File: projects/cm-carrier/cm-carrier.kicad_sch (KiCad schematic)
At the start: 0 parts

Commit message: cm-carrier: power sheet (XA 5V input, TPS62132 3.3V/3A for LTE)
Co-Authored-By: Claude Opus 5.5 <noreply@anthropic.com>
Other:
- added sheet Power (power.kicad_sch)
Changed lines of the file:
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@@
 	(generator_version "10.0")
 	(paper "A4")
+  (sheet
+    (at 30 30)
+    (size 40 25)
+    (exclude_from_sim no)
+    (in_bom yes)
+    (on_board yes)
+    (dnp no)
+    (fields_autoplaced yes)
+    (stroke (width 0.1524) (type solid))
+    (fill (color 0 0 0 0.0))
+    (property "Sheetname" "Power"
+      (at 30 29.365 0)
+      (show_name no)
+      (do_not_autoplace no)
+      (effects (font (size 1.27 1.27)) (justify left bottom))
+    )
+    (property "Sheetfile" "power.kicad_sch"
+      (at 30 55.635 0)
+      (show_name no)
+      (do_not_autoplace no)
+      (effects (font (size 1.27 1.27)) (justify left top))
+    )
+    (instances
+      (project "cm-carrier"
+        (path "/a976657b-65a0-4cc4-bafb-6280c56b6145" (page "2"))
+      )
+    )
+  )
+  (sheet_instances
+    (path "/"
+      (page "1")
+    )
+  )
+  (embedded_fonts no)
 )

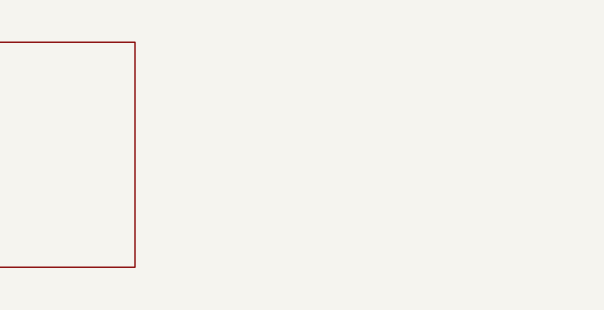
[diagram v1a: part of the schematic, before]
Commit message: cm-carrier: CM sheet (CM4/CM5 module, debug UART, ACT LED, power button)
Co-Authored-By: Claude Opus 5.5 <noreply@anthropic.com>
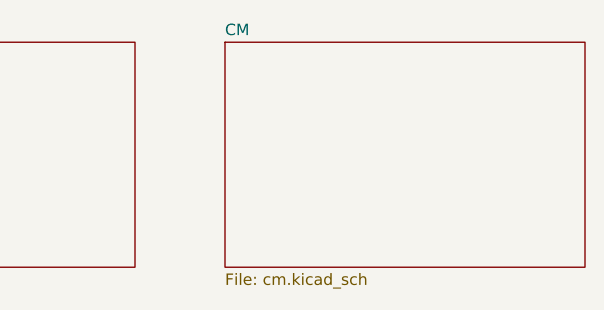
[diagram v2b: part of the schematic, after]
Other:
- added sheet CM (cm.kicad_sch)
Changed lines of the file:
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@@
+    )
+  )
+  (sheet
+    (at 80 30)
+    (size 40 25)
+    (exclude_from_sim no)
+    (in_bom yes)
+    (on_board yes)
+    (dnp no)
+    (fields_autoplaced yes)
+    (stroke (width 0.1524) (type solid))
+    (fill (color 0 0 0 0.0))
+    (property "Sheetname" "CM"
+      (at 80 29.365 0)
+      (show_name no)
+      (do_not_autoplace no)
+      (effects (font (size 1.27 1.27)) (justify left bottom))
+    )
+    (property "Sheetfile" "cm.kicad_sch"
+      (at 80 55.635 0)
+      (show_name no)
+      (do_not_autoplace no)
+      (effects (font (size 1.27 1.27)) (justify left top))
+    )
+    (instances
+      (project "cm-carrier"
+        (path "/a976657b-65a0-4cc4-bafb-6280c56b6145" (page "3"))
+      )
     )
   )

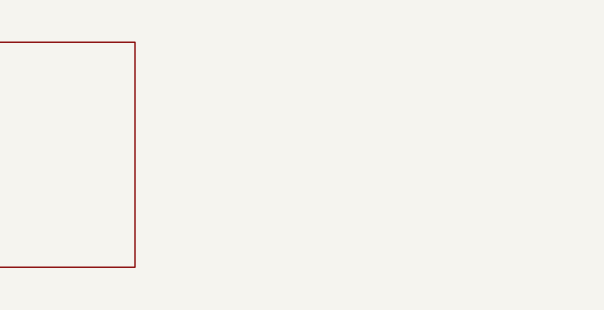
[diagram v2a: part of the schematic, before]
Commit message: cm-carrier: USB hub sheet (USB2514B, 3 switched ports: Type-C + 2x XA); open-issues list
Co-Authored-By: Claude Opus 5.5 <noreply@anthropic.com>
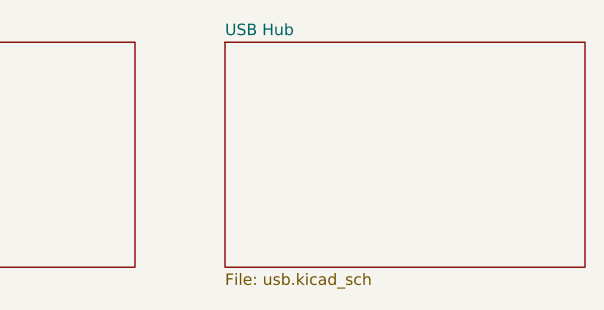
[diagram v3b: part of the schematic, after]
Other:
- added sheet USB Hub (usb.kicad_sch)
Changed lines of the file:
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@@
+    )
+  )
+  (sheet
+    (at 130 30)
+    (size 40 25)
+    (exclude_from_sim no)
+    (in_bom yes)
+    (on_board yes)
+    (dnp no)
+    (fields_autoplaced yes)
+    (stroke (width 0.1524) (type solid))
+    (fill (color 0 0 0 0.0))
+    (property "Sheetname" "USB Hub"
+      (at 130 29.365 0)
+      (show_name no)
+      (do_not_autoplace no)
+      (effects (font (size 1.27 1.27)) (justify left bottom))
+    )
+    (property "Sheetfile" "usb.kicad_sch"
+      (at 130 55.635 0)
+      (show_name no)
+      (do_not_autoplace no)
+      (effects (font (size 1.27 1.27)) (justify left top))
+    )
+    (instances
+      (project "cm-carrier"
+        (path "/a976657b-65a0-4cc4-bafb-6280c56b6145" (page "4"))
+      )
     )
   )

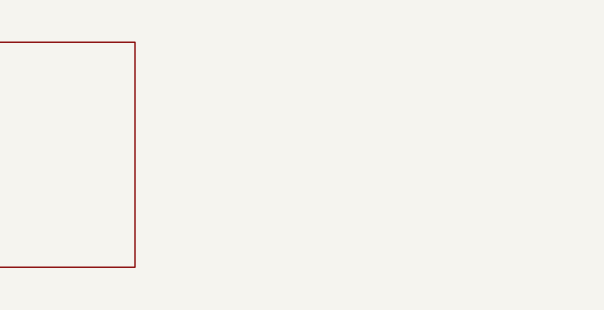
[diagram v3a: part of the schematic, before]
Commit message: cm-carrier: LTE sheet (EC25-J Mini PCIe, nanoSIM, open-drain PERST#/W_DISABLE#); move LTE control to GPIO22/23
Co-Authored-By: Claude Opus 5.5 <noreply@anthropic.com>
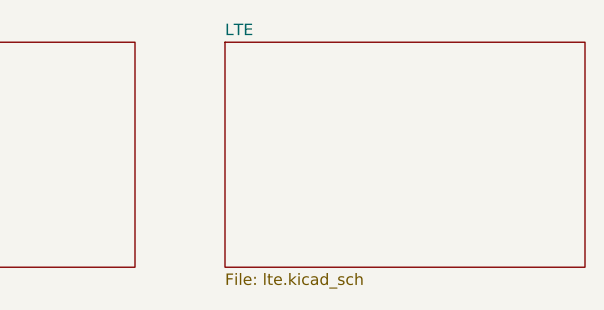
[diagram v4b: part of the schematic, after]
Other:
- added sheet LTE (lte.kicad_sch)
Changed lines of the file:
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@@
+    )
+  )
+  (sheet
+    (at 180 30)
+    (size 40 25)
+    (exclude_from_sim no)
+    (in_bom yes)
+    (on_board yes)
+    (dnp no)
+    (fields_autoplaced yes)
+    (stroke (width 0.1524) (type solid))
+    (fill (color 0 0 0 0.0))
+    (property "Sheetname" "LTE"
+      (at 180 29.365 0)
+      (show_name no)
+      (do_not_autoplace no)
+      (effects (font (size 1.27 1.27)) (justify left bottom))
+    )
+    (property "Sheetfile" "lte.kicad_sch"
+      (at 180 55.635 0)
+      (show_name no)
+      (do_not_autoplace no)
+      (effects (font (size 1.27 1.27)) (justify left top))
+    )
+    (instances
+      (project "cm-carrier"
+        (path "/a976657b-65a0-4cc4-bafb-6280c56b6145" (page "5"))
+      )
     )
   )

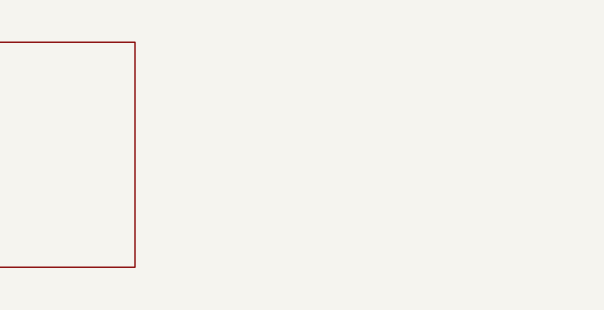
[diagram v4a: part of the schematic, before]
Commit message: cm-carrier: IO sheet (GbE MagJack, micro HDMI with ESD, microSD); ERC clean
Co-Authored-By: Claude Opus 5.5 <noreply@anthropic.com>
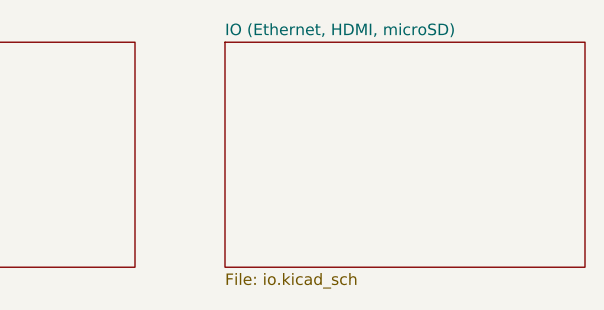
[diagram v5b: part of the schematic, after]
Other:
- added sheet IO (Ethernet, HDMI, microSD) (io.kicad_sch)
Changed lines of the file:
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@@
+    )
+  )
+  (sheet
+    (at 230 30)
+    (size 40 25)
+    (exclude_from_sim no)
+    (in_bom yes)
+    (on_board yes)
+    (dnp no)
+    (fields_autoplaced yes)
+    (stroke (width 0.1524) (type solid))
+    (fill (color 0 0 0 0.0))
+    (property "Sheetname" "IO (Ethernet, HDMI, microSD)"
+      (at 230 29.365 0)
+      (show_name no)
+      (do_not_autoplace no)
+      (effects (font (size 1.27 1.27)) (justify left bottom))
+    )
+    (property "Sheetfile" "io.kicad_sch"
+      (at 230 55.635 0)
+      (show_name no)
+      (do_not_autoplace no)
+      (effects (font (size 1.27 1.27)) (justify left top))
+    )
+    (instances
+      (project "cm-carrier"
+        (path "/a976657b-65a0-4cc4-bafb-6280c56b6145" (page "6"))
+      )
     )
   )
